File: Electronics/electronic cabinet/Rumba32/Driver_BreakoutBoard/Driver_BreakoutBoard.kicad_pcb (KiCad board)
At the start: 2 copper layers, 15.2 x 29.2 mm, 14 parts, among them IC1 SN74ACT32PWR, J1 Conn_01x08, J2 Conn_01x08, J3 Conn_01x02, J4 0393570002, J5 Conn_01x02, Q1 Q_NPN_CEB

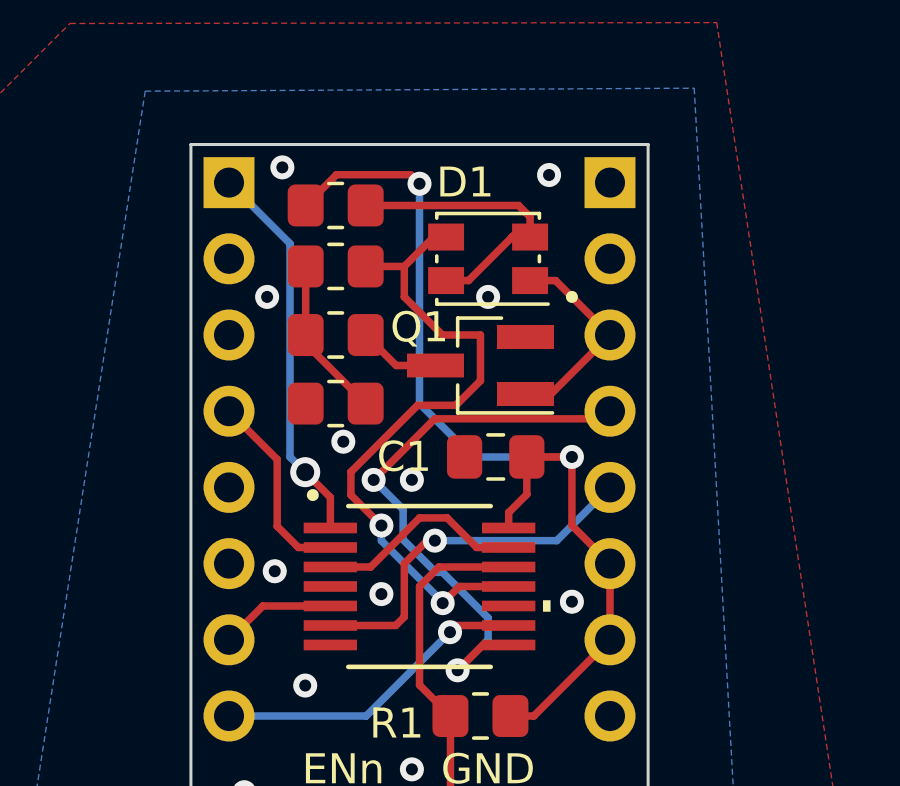
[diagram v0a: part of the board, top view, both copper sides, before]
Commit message: Updated with new PCB Layout.
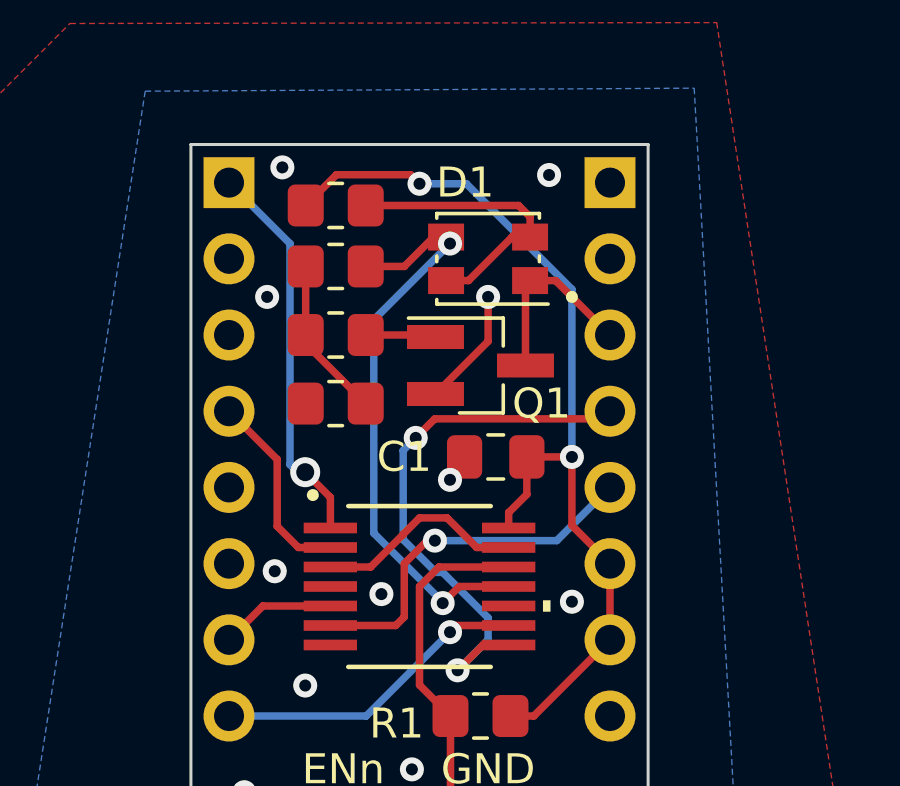
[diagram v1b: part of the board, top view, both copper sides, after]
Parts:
- turned Q1 to 0 degrees
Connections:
- Q1 pad 1: /EN- -> Net-(Q1-Pad1)
- Q1 pad 3: Net-(Q1-Pad3) -> /EN-
- R4 pad 2: Net-(Q1-Pad3) -> Net-(Q1-Pad1)
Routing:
- net GND: track 0.00 -> 3.96 mm, vias 12 -> 11
- net Net-(D1-Pad3): track 22.3 -> 19.5 mm
- net Net-(Q1-Pad3): track 2.75 -> 0.00 mm
- net Net-(Q1-Pad1): track 0.00 -> 2.35 mm
- net +5V: track 32.6 -> 31.6 mm
- net /DIR-: track 19.4 -> 18.5 mm
- net /EN-: track 7.05 -> 6.53 mm

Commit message: Small improvement to board layout.
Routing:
- net GND: track 3.96 -> 0.00 mm
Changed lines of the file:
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@@
   (segment (start 137.7055 86.9055) (end 141.224 90.424) (width 0.25) (layer "B.Cu") (net 1))
   (segment (start 141.224 90.424) (end 141.224 96.012) (width 0.25) (layer "B.Cu") (net 1))
-  (segment (start 136.676 93.914) (end 138.43 92.16) (width 0.25) (layer "F.Cu") (net 2))
-  (segment (start 138.43 92.16) (end 138.43 90.678) (width 0.25) (layer "F.Cu") (net 2))
   (via (at 140.462 86.614) (size 0.8) (drill 0.4) (layers "F.Cu" "B.Cu") (free) (net 2))
   (via (at 137.16 96.774) (size 0.8) (drill 0.4) (layers "F.Cu" "B.Cu") (free) (net 2))
